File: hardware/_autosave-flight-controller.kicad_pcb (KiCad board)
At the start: 4 copper layers, 70 x 70 mm, 117 parts, among them J1 USB_C_Receptacle_USB2.0_16P, J10 Screw_Terminal_01x02, J11 Micro_SD_Card_Det_Hirose_DM3AT, J12 Conn_01x03, J13 Conn_01x03, J14 Conn_01x03, J15 Conn_01x03, J16 Screw_Terminal_01x02, J17 Conn_01x04, J18 Screw_Terminal_01x02, J19 Conn_01x02, J2 Conn_01x02, J20 Conn_01x02, J21 Conn_01x02, J22 Conn_01x02, J23 Conn_01x02, J3 Conn_Coaxial, J4 Conn_01x04, J5 Screw_Terminal_01x02, J6 Conn_01x04, J7 Screw_Terminal_01x02, J8 Conn_01x04, J9 Screw_Terminal_01x02, U1 BMP384, U2 LSM6DSOTR, U3 MMC5983MA, U4 NEO-M9N, U5 TPS2121RUXR, U6 AP62300TWU, U7 STM32H723VGTx, Y1 Q13FC13500004, Y2 X322525MOB4SI

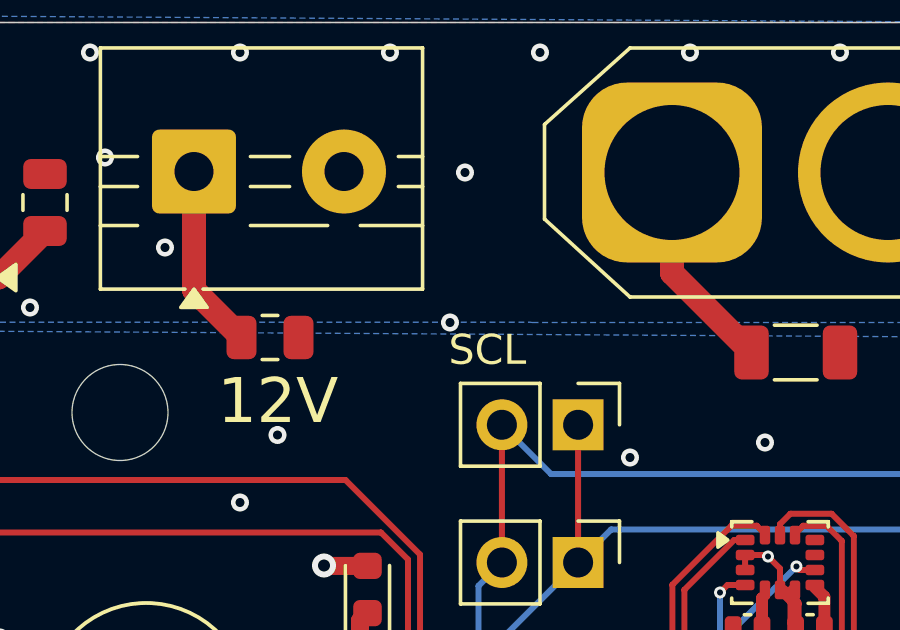
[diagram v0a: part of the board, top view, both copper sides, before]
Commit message: added seperate I2C channel
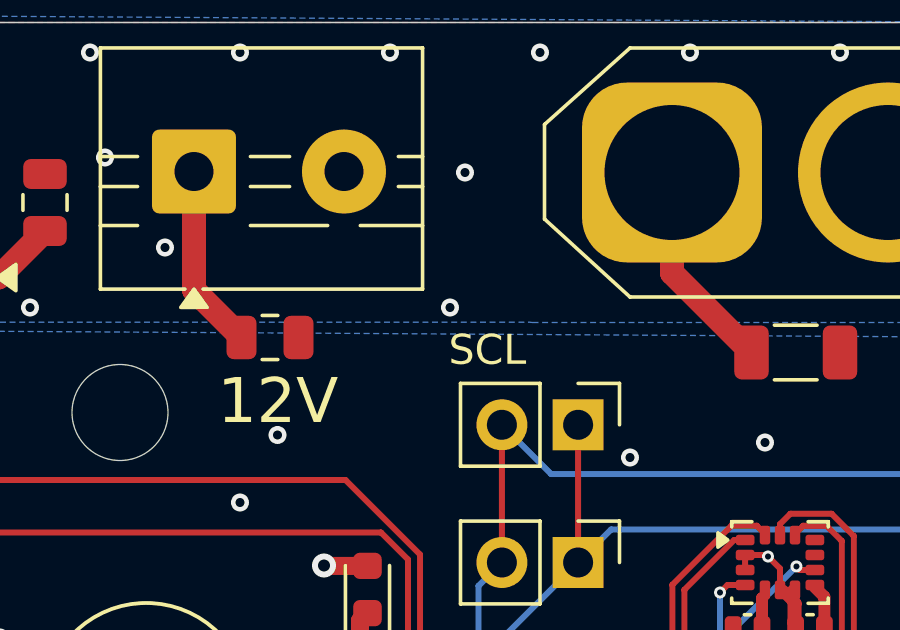
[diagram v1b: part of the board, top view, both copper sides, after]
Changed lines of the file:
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@@
 	)
 	(via
-		(at 131 78)
+		(at 131 77.5)
 		(size 0.6)
 		(drill 0.3)
